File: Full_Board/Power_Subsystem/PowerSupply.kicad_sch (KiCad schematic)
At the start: 0 parts

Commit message: Worked on Power supply subsheet
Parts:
- added C? (x5): C, symbol Device:C
- added D?: D_Zener, symbol Device:D_Zener
- added J1: KLDHCX-8-0202-A, KLDHCX80202A, symbol KLDHCX-8-0202-A:KLDHCX-8-0202-A
- added L?: L, symbol Device:L
- added R? (x2): R, symbol Device:R
- added TP1, TP2, TP3, TP4: TestPoint, TestPoint:TestPoint_Keystone_5010-5014_Multipurpose, symbol Connector:TestPoint
- added U?: TPS5403DR, D0008A_N, symbol TPS5403DR:TPS5403DR
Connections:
- new net: R?.1, U?.6 (COMP)
- new net: C?.1, R?.2
- new net: C?.2, U?.1 (BOOT)
- new net: R?.2, U?.3 (ROSC)
- new net: C?.1, U?.4 (SS)
- new net: C?.1, D?.1 (K), L?.1, U?.8 (LX)
- new net +24V: C?.2, J1.2, TP4.1, U?.2 (VIN)
- new net +3.3V: C?.1, L?.2, U?.5 (VSENSE)
- new net GND: C?.1, C?.2, C?.2, C?.2, D?.2 (A), J1.1, R?.1, TP1.1, TP2.1, TP3.1, U?.7 (GND)
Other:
- note added: "Barrel Jack Connector"
- note added: "DC-DC Converter (24 -> 3.3V)"
- note added: "I think pins 3 and 4 on the barrel jack are mounting, not electrical"

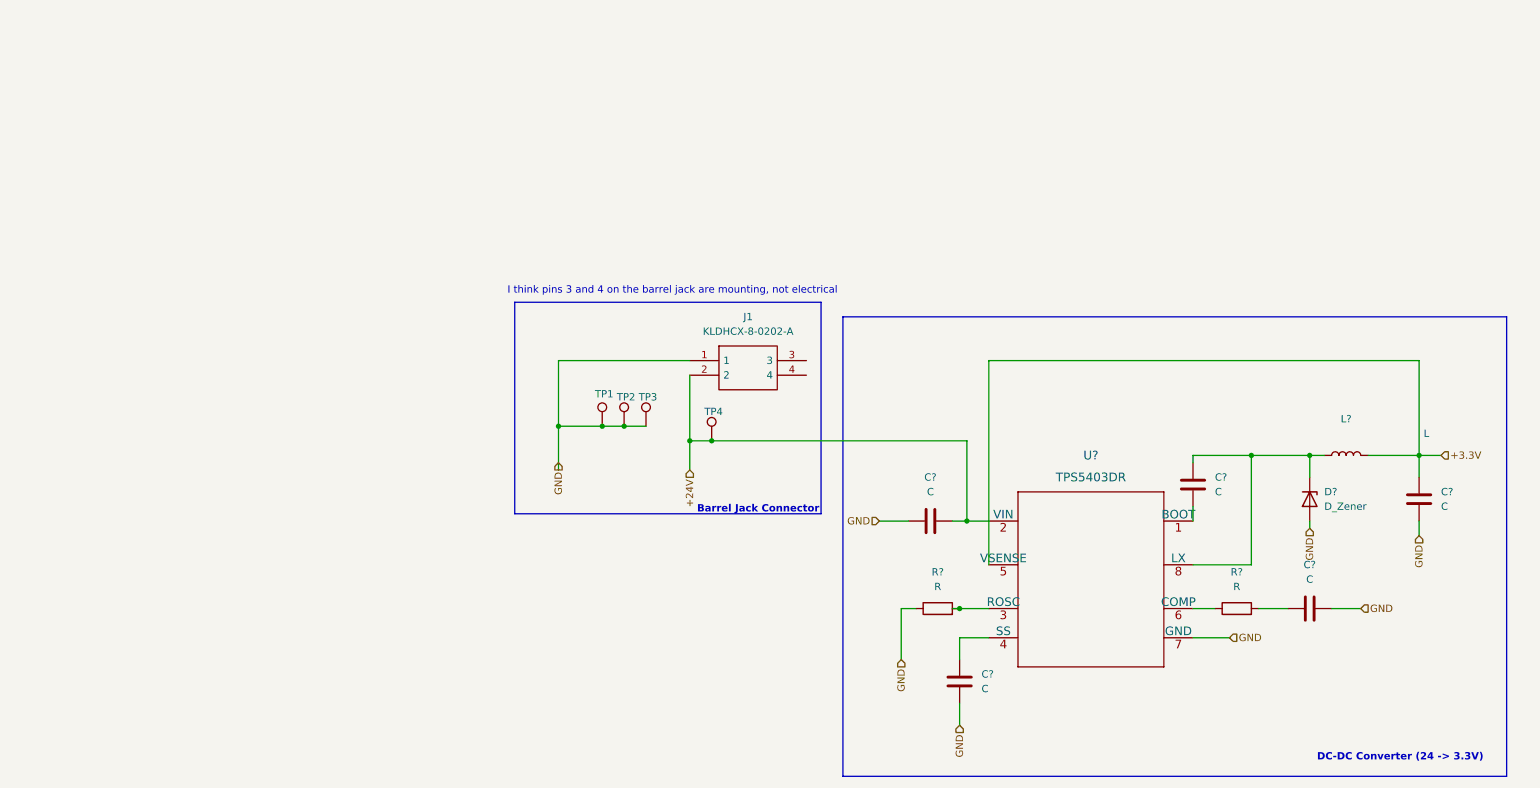
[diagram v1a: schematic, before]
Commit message: Finalize MSP432, stepper, and button subsheets
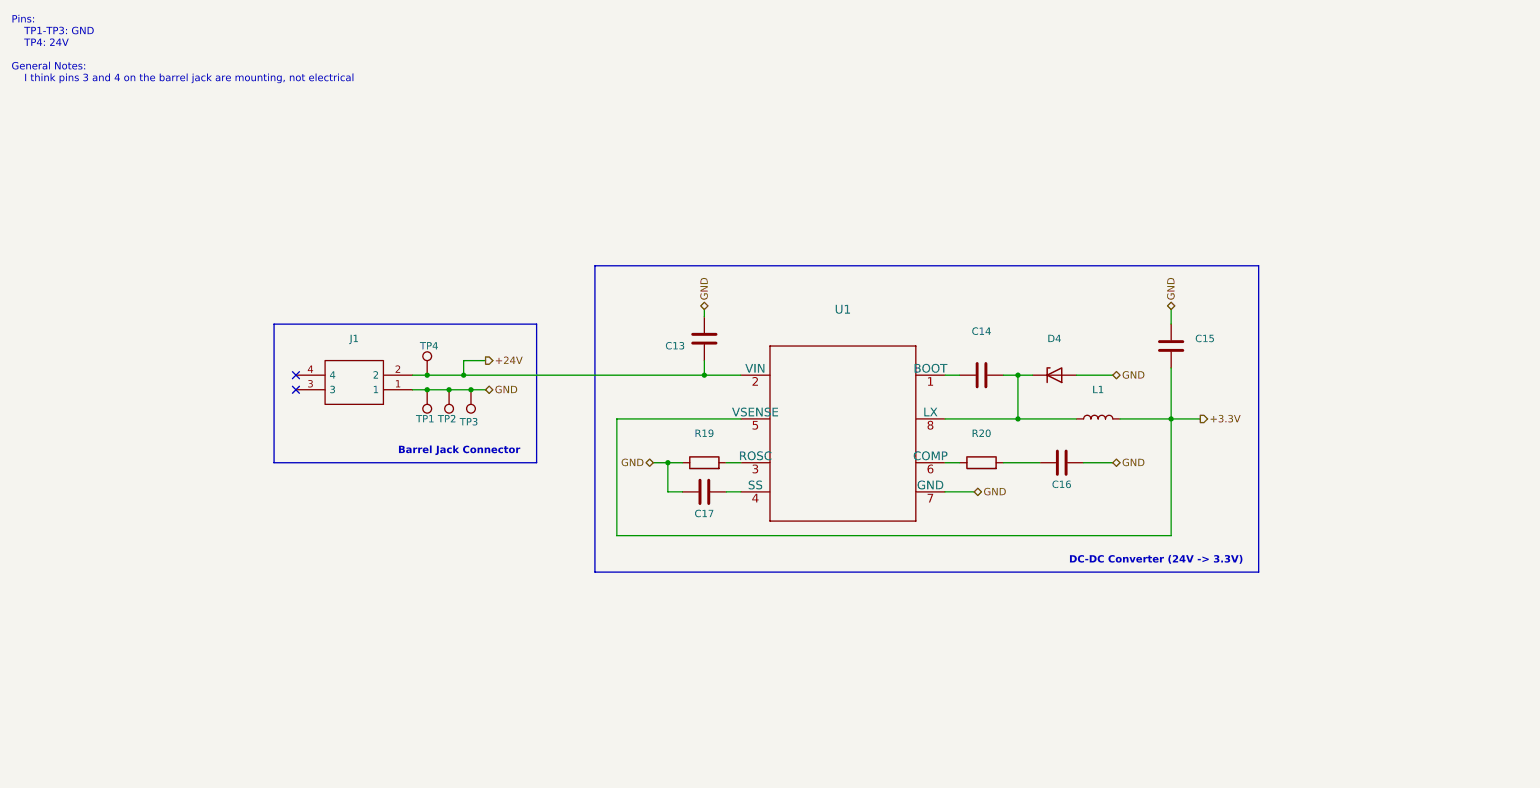
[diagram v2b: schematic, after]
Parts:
- C13, C14, C15, C16, C17: renamed from C?; value C -> ~
- D4: renamed from D?; value D_Zener -> ~
- J1: value KLDHCX-8-0202-A -> (none); footprint KLDHCX80202A -> (none); Digikey Part Number (none) -> 2092-KLDHCX-8-0202-A-ND; Digikey link (none) -> https://www.digikey.in/en/products/detail/kycon-inc/KLDHCX-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; Manufacturer's Part Number (none) -> KLDHCX-8-0202-A; Mouser link (none) -> https://www.mouser.com/ProductDetail/Kycon/KLDHCX-8-0202-A?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
- L1: renamed from L?; value L -> ~
- R19, R20: renamed from R?; value R -> (none)
- TP1: renamed from TP3; value TestPoint -> ~; footprint TestPoint:TestPoint_Keystone_5010-5014_Multipurpose -> (none)
- TP2: value TestPoint -> ~; footprint TestPoint:TestPoint_Keystone_5010-5014_Multipurpose -> (none)
- TP3: renamed from TP1; value TestPoint -> ~; footprint TestPoint:TestPoint_Keystone_5010-5014_Multipurpose -> (none)
- TP4: value TestPoint -> (none); footprint TestPoint:TestPoint_Keystone_5010-5014_Multipurpose -> (none)
- U1: renamed from U?; value TPS5403DR -> (none)
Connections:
- net +24V: now also C13.1; no longer C13.2
- net GND: now also C13.2, C17.1; no longer C13.1, C17.2
- net at U1.1 (BOOT): now also C14.1; no longer C14.2
- net at U1.4 (SS): now also C17.2; no longer C17.1
- net at D4.1 (K), L1.1, U1.8 (LX): now also C14.2; no longer C14.1
- no-connect marks 0 -> 2
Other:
- note added: "DC-DC Converter (24V -> 3.3V)"
- note added: "Pins: TP1-TP3: GND TP4: 24V General Notes: I think pins 3 and 4 on the barrel jack are mounting, not electrical"
- note removed: "DC-DC Converter (24 -> 3.3V)"
- note removed: "I think pins 3 and 4 on the barrel jack are mounting, not electrical"
- moved on the sheet: C13, C14, C15, C16, C17, D4, J1, L1, R19, R20, TP1, TP2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

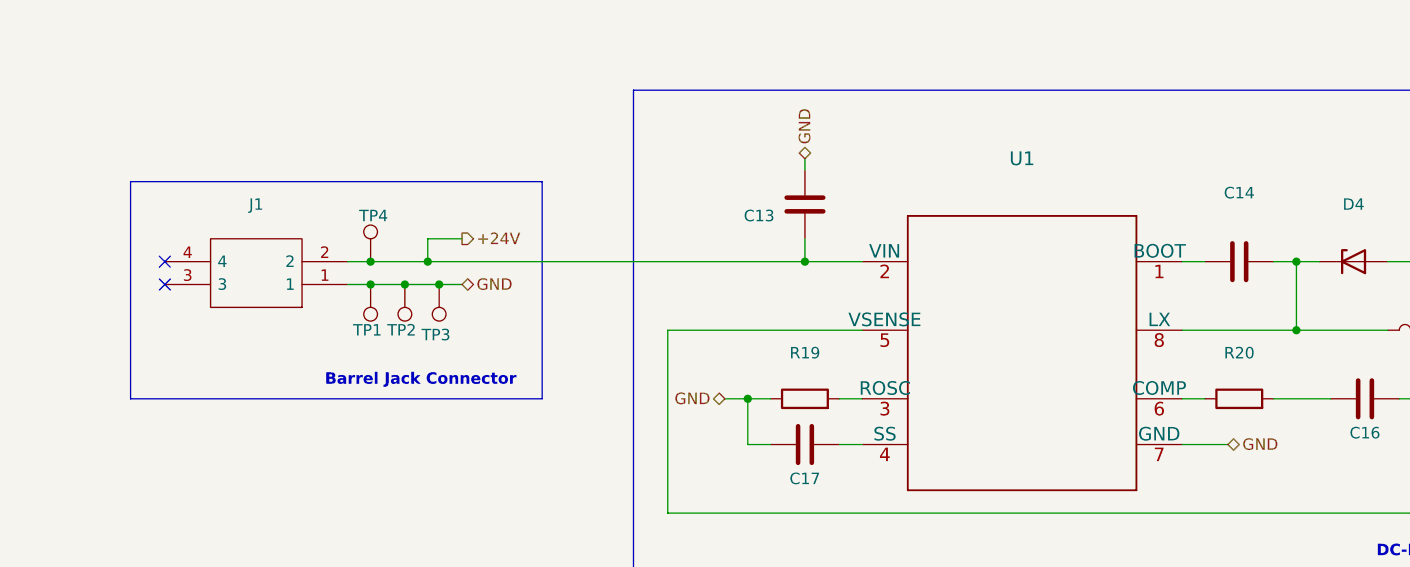
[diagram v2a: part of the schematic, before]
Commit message: Layout LED subsystem
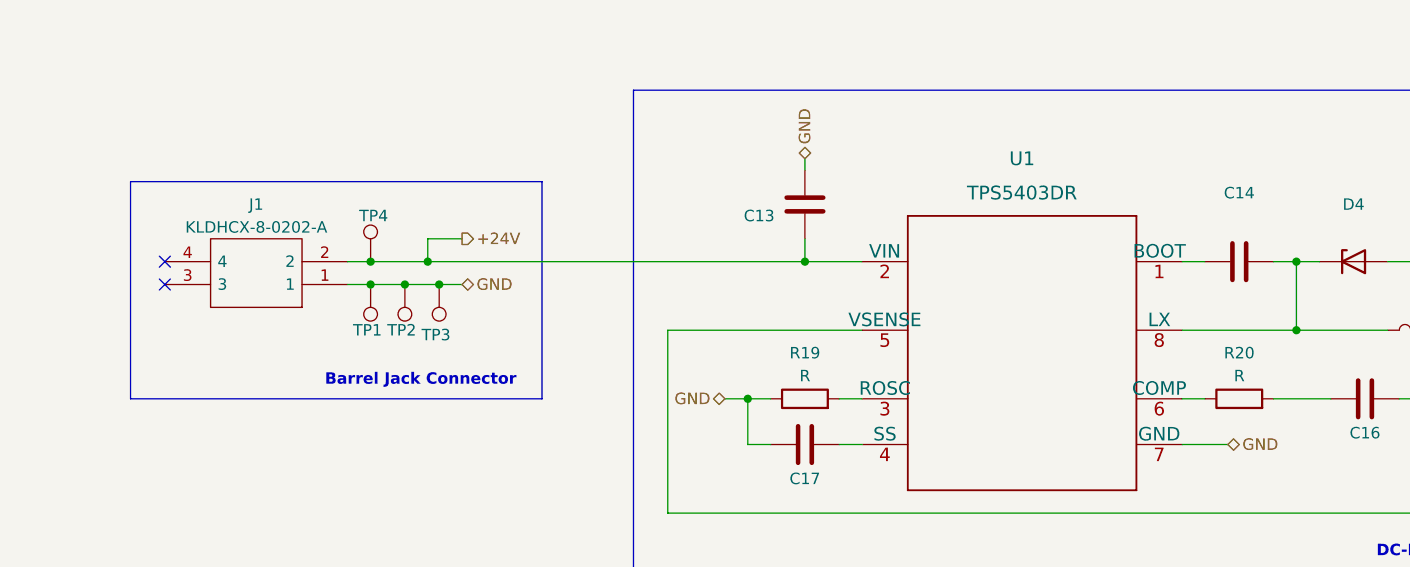
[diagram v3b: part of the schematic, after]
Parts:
- J1: value (none) -> KLDHCX-8-0202-A; footprint (none) -> KLDHCX80202A
- R19, R20: value (none) -> R
- TP4: value (none) -> TestPoint; footprint (none) -> TestPoint:TestPoint_Keystone_5010-5014_Multipurpose
- U1: value (none) -> TPS5403DR
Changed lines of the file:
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@@
     (in_bom yes) (on_board yes)
     (property "Reference" "R20" (id 0) (at 185.42 90.17 90))
-    (property "Value" "" (id 1) (at 185.42 92.71 90))
+    (property "Value" "R" (id 1) (at 185.42 92.71 90))
     (property "Footprint" "" (id 2) (at 185.42 97.028 90)
       (effects (font (size 1.27 1.27)) hide)
@@
       (effects (font (size 1.524 1.524)))
     )
-    (property "Value" "" (id 1) (at 161.29 72.39 0)
+    (property "Value" "TPS5403DR" (id 1) (at 161.29 72.39 0)
       (effects (font (size 1.524 1.524)))
     )
@@
     (in_bom yes) (on_board yes)
     (property "Reference" "J1" (id 0) (at 76.2 73.66 0))
-    (property "Value" "" (id 1) (at 76.2 76.2 0))
-    (property "Footprint" "" (id 2) (at 69.85 85.09 0)
+    (property "Value" "KLDHCX-8-0202-A" (id 1) (at 76.2 76.2 0))
+    (property "Footprint" "KLDHCX80202A" (id 2) (at 69.85 85.09 0)
       (effects (font (size 1.27 1.27)) (justify left) hide)
     )
@@
       (effects (font (size 1.27 1.27)) (justify left))
     )
-    (property "Value" "" (id 1) (at 91.44 77.9779 0)
-      (effects (font (size 1.27 1.27)) (justify left) hide)
-    )
-    (property "Footprint" "" (id 2) (at 93.98 80.01 0)
+    (property "Value" "TestPoint" (id 1) (at 91.44 77.9779 0)
+      (effects (font (size 1.27 1.27)) (justify left) hide)
+    )
+    (property "Footprint" "TestPoint:TestPoint_Keystone_5010-5014_Multipurpose" (id 2) (at 93.98 80.01 0)
       (effects (font (size 1.27 1.27)) hide)
     )
@@
     (in_bom yes) (on_board yes)
     (property "Reference" "R19" (id 0) (at 137.16 90.17 90))
-    (property "Value" "" (id 1) (at 137.16 92.71 90))
+    (property "Value" "R" (id 1) (at 137.16 92.71 90))
     (property "Footprint" "" (id 2) (at 137.16 97.028 90)
       (effects (font (size 1.27 1.27)) hide)

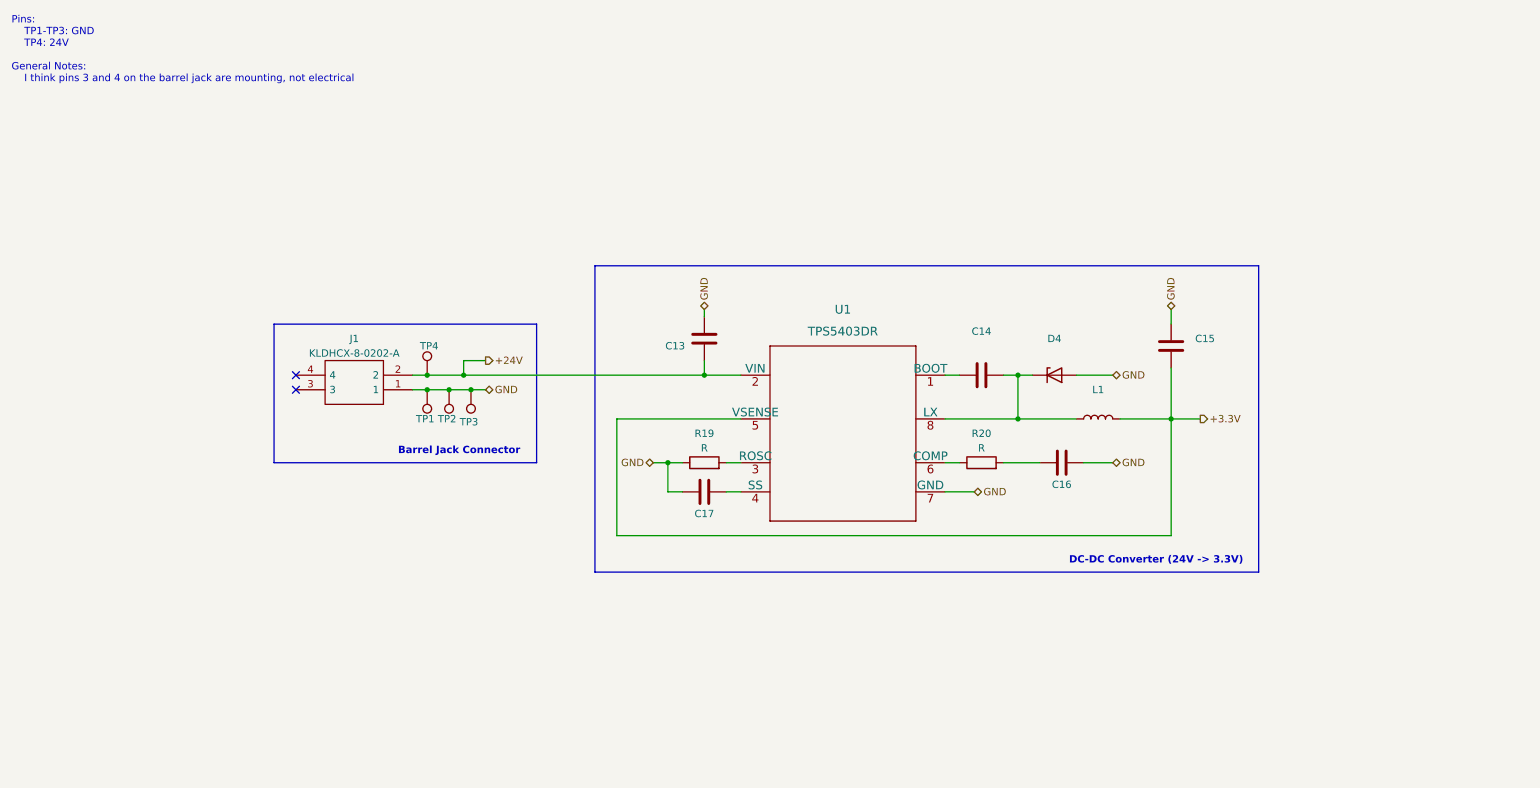
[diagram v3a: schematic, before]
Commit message: Changed the DC convertor circuit
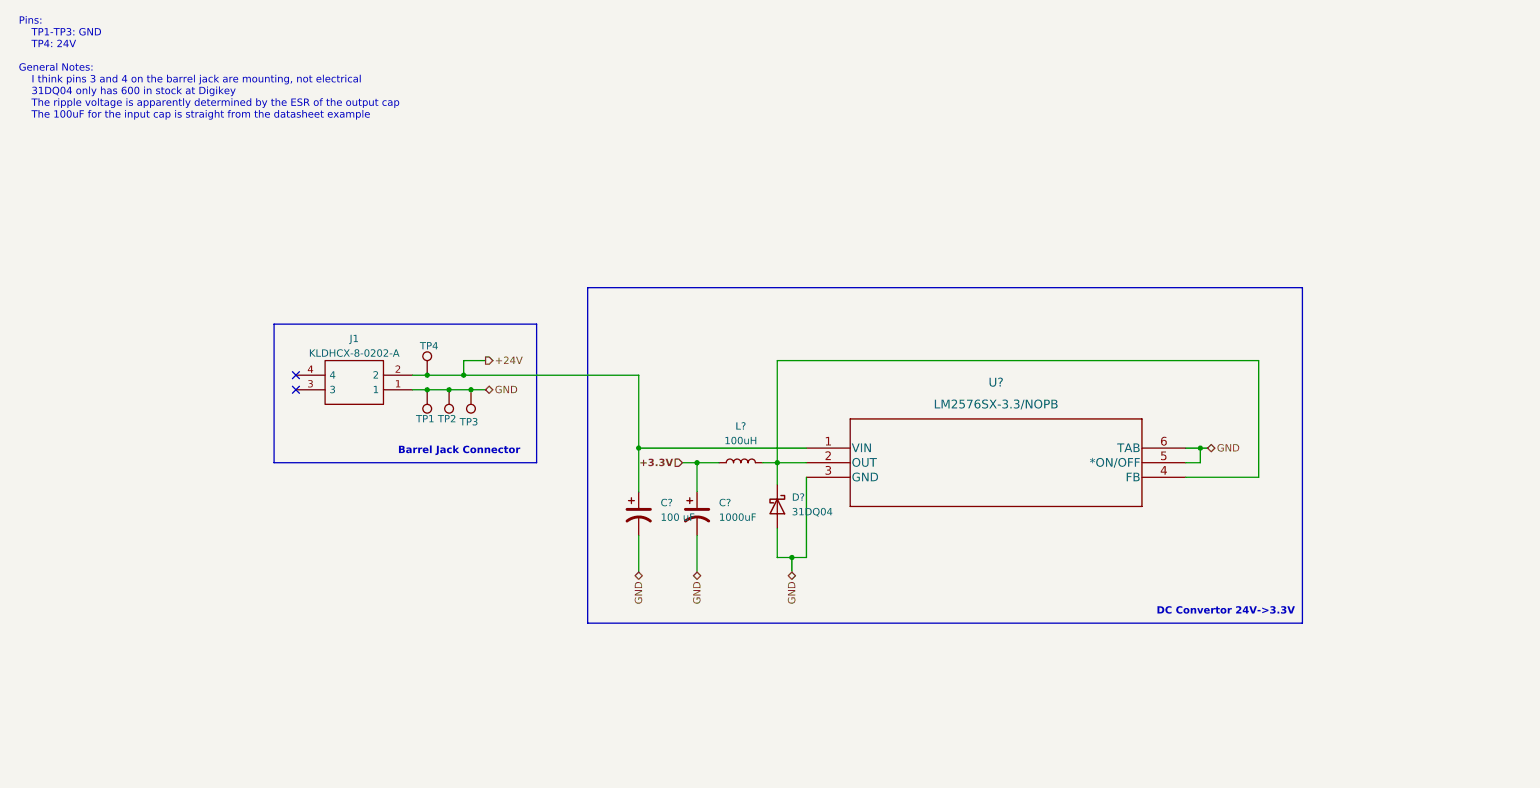
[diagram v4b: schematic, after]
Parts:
- removed C13, C14, C15, C16, C17: ~, symbol Device:C
- removed D4: ~, symbol Device:D_Zener
- removed L1: ~, symbol Device:L
- removed R19, R20: R, symbol Device:R
- removed U1: TPS5403DR, D0008A_N, symbol TPS5403DR:TPS5403DR
- added C?: 100 uF, symbol Device:C_Polarized_US
- added C?: 1000uF, symbol Device:C_Polarized_US
- added D?: 31DQ04, symbol Device:D_Schottky
- added L?: 100uH, symbol Device:L
- added U?: LM2576SX-3.3/NOPB, TS5B_TEX, symbol LM25776SX-3-3-NOPB:LM2576SX-3.3/NOPB
- TP1, TP2, TP3: footprint (none) -> TestPoint:TestPoint_Keystone_5010-5014_Multipurpose
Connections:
- net +24V: now also C?.1, U?.1 (VIN)
- net +3.3V: now also C?.1, L?.1
- net GND: now also C?.2, C?.2, D?.2 (A), U?.3 (GND), U?.5 (*ON/OFF), U?.6 (TAB)
- new net: D?.1 (K), L?.2, U?.2 (OUT), U?.4 (FB)
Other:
- note added: "DC Convertor 24V->3.3V"
- note added: "Pins: TP1-TP3: GND TP4: 24V General Notes: I think pins 3 and 4 on the barrel jack are mounting, not electrical 31DQ04 only has 600 in stock at Digikey The ripple voltage is apparently determined by the ESR of the output cap The 100uF for the input cap is straight from the datasheet example"
- note removed: "DC-DC Converter (24V -> 3.3V)"
- note removed: "Pins: TP1-TP3: GND TP4: 24V General Notes: I think pins 3 and 4 on the barrel jack are mounting, not electrical"
